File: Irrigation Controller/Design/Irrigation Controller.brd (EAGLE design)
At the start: 100 x 80 mm, 21 parts, among them IC1 7809DT, IC2 LM1117-3.3, IC3 7805DT, U1 ESP-WROOM-32, U4 MB6S

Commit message: Updated Schematics and Board
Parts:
- added D2, D3, D4, D5: (no value), diode:SOD123
- added JP1: Serial, SpaceDIY_connectors:1X04
- added OK1, OK2, OK3, OK4: SFH6186-4, optocoupler:SMD4-7
- added R10, R7, R8, R9: 470, resistor:R1206
- added R11: 10k, SpaceDIY_passive_components:1206
- added R3, R4, R5, R6: 10K, resistor:R1206
- added S3, S4, S5: 219-08, switch-dil:CTS-219-08
- added T1, T2, T3, T4: BC847, transistor:SOT23
- added U$6: SWITCH_SPDT, SparkFun-Retired:KPS-1290
- added X1, X2, X3, X4: 22-23-2021, con-molex:22-23-2021
- U1: value ESP-WROOM-32 -> ESP-32S; device esp32:ESP-WROOM-32 -> esp32:ESP-32S
- moved D1 188.2 mm to (21.0, 101.0)
- moved C6 149.5 mm to (54.0, 86.0)
- moved C2 148.9 mm to (41.0, 92.0)
- moved C3 148.9 mm to (47.0, 92.0)
- moved C5 148.9 mm to (47.0, 86.0)
- moved S2 2.83 mm to (13.0, 32.0)
- moved U$3 2.24 mm to (37.0, 17.0)
- moved U$2 1.41 mm to (13.0, 17.0)
- moved U$4 1.41 mm to (62.0, 17.0)
- moved U$5 1.00 mm to (86.0, 17.0)
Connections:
- removed net VCC: R2.2
- new net 2R1: S3.10, S3.11, S3.12, S3.14, S3.16, X2.1
- new net 2R2: S3.13, S3.15, S3.9, U$3.SWCOMMON
- new net 3R1: S4.10, S4.11, S4.12, S4.14, S4.16, X3.1
- new net 3R2: S4.13, S4.15, S4.9, U$4.SWCOMMON
- new net 4R1: S5.10, S5.11, S5.12, S5.14, S5.16, X4.1
- new net 4R2: S5.13, S5.15, S5.9, U$5.SWCOMMON
- new net CLK: U1.20
- new net CMD: U1.19
- new net IO0: R11.2, U$6.P, U1.25
- new net IO12: U1.14
- new net IO13: U1.16
- new net IO14: U1.13
- new net IO15: U1.23
- new net IO16: U1.27
- new net IO17: U1.28
- new net IO18: U1.30
- new net IO19: U1.31
- new net IO2: U1.24
- new net IO21: U1.33
- new net IO22: U1.36
- new net IO23: U1.37
- new net IO25: U1.10
- new net IO26: U1.11
- new net IO27: U1.12
- new net IO32: U1.8
- new net IO33: U1.9
- new net IO34: U1.6
- new net IO35: U1.7
- new net IO4: U1.26
- new net IO5: U1.29
- new net N$1: U$5.SWOPEN, X4.2
- new net N$10: D3.C, OK2.4, U$3.COIL1
- new net N$11: D3.A, T2.3, U$3.COIL0
- new net N$12: OK2.3, R4.2
- new net N$13: R4.1, T2.1
- new net N$14: D4.C, OK3.4, U$4.COIL1
- new net N$15: D4.A, T3.3, U$4.COIL0
- new net N$16: OK3.3, R5.2
- new net N$17: R5.1, T3.1
- new net N$18: D5.C, OK4.4, U$5.COIL1
- new net N$19: D5.A, T4.3, U$5.COIL0
- new net N$2: U$4.SWOPEN, X3.2
- new net N$20: OK4.3, R6.2
- new net N$21: R6.1, T4.1
- new net N$22: OK1.1, R7.1
- new net N$23: R7.2
- new net N$25: OK2.1, R8.1
- new net N$26: R8.2
- new net N$27: OK3.1, R9.1
- new net N$28: R9.2
- new net N$29: OK4.1, R10.1
- new net N$30: R10.2
- new net N$4: U$3.SWOPEN, X2.2
- new net N$5: U$2.SWOPEN, X1.2
- new net N$6: D2.C, OK1.4, U$2.COIL1
- new net N$7: D2.A, T1.3, U$2.COIL0
- new net N$8: OK1.3, R3.2
- new net N$9: R3.1, T1.1
- new net RX: JP1.1, U1.34
- new net SD0: U1.21
- new net SD1: U1.22
- new net SD2: U1.17
- new net SD3: U1.18
- new net SVN: U1.5
- new net SVP: U1.4
- new net TX: JP1.2, U1.35
- net 1R1: now also X1.1
- net 1R2: now also U$2.SWCOMMON
- net 24V1: now also S3.3, S4.3, S5.3
- net 24V2: now also S3.4, S4.4, S5.4
- net 3V3: now also R11.1, R2.2, S3.7, S4.7, S5.7
- net 5V: now also JP1.4, S3.6, S4.6, S5.6
- net 9V: now also S3.5, S4.5, S5.5
- net AC1: now also S3.1, S4.1, S5.1
- net AC2: now also S3.2, S4.2, S5.2
- net GND: now also JP1.3, OK1.2, OK2.2, OK3.2, OK4.2, S3.8, S4.8, S5.8, T1.2, T2.2, T3.2, T4.2, U$6.O
- net RST: now also U1.3

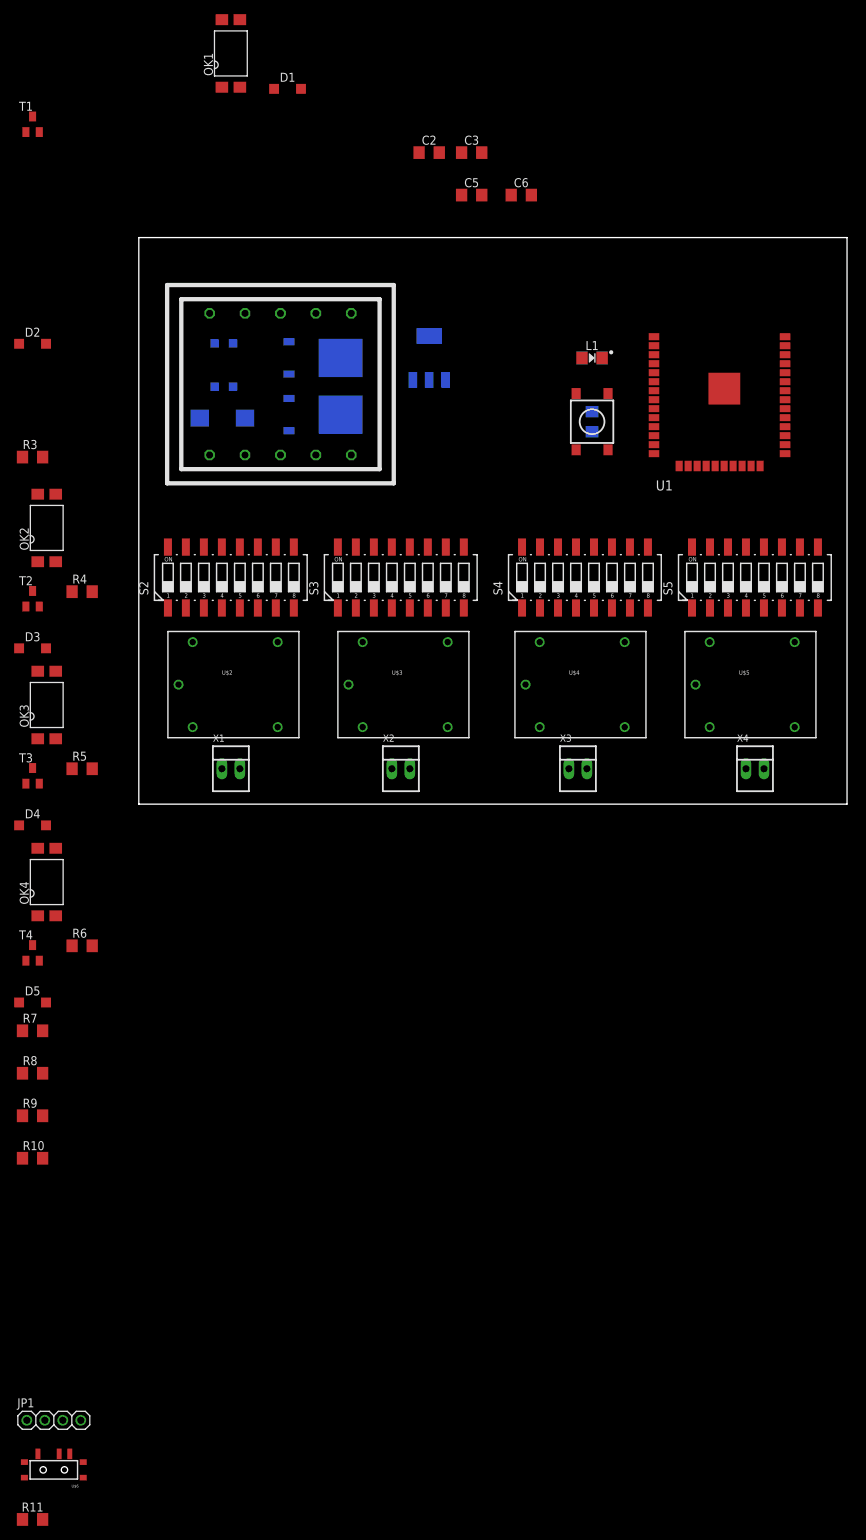
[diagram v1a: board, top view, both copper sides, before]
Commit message: Irrigation controller with support for:  * 220 VAC  * 24 VAC  * 9 VDC  * 5 VDC  * 3.3 VDC
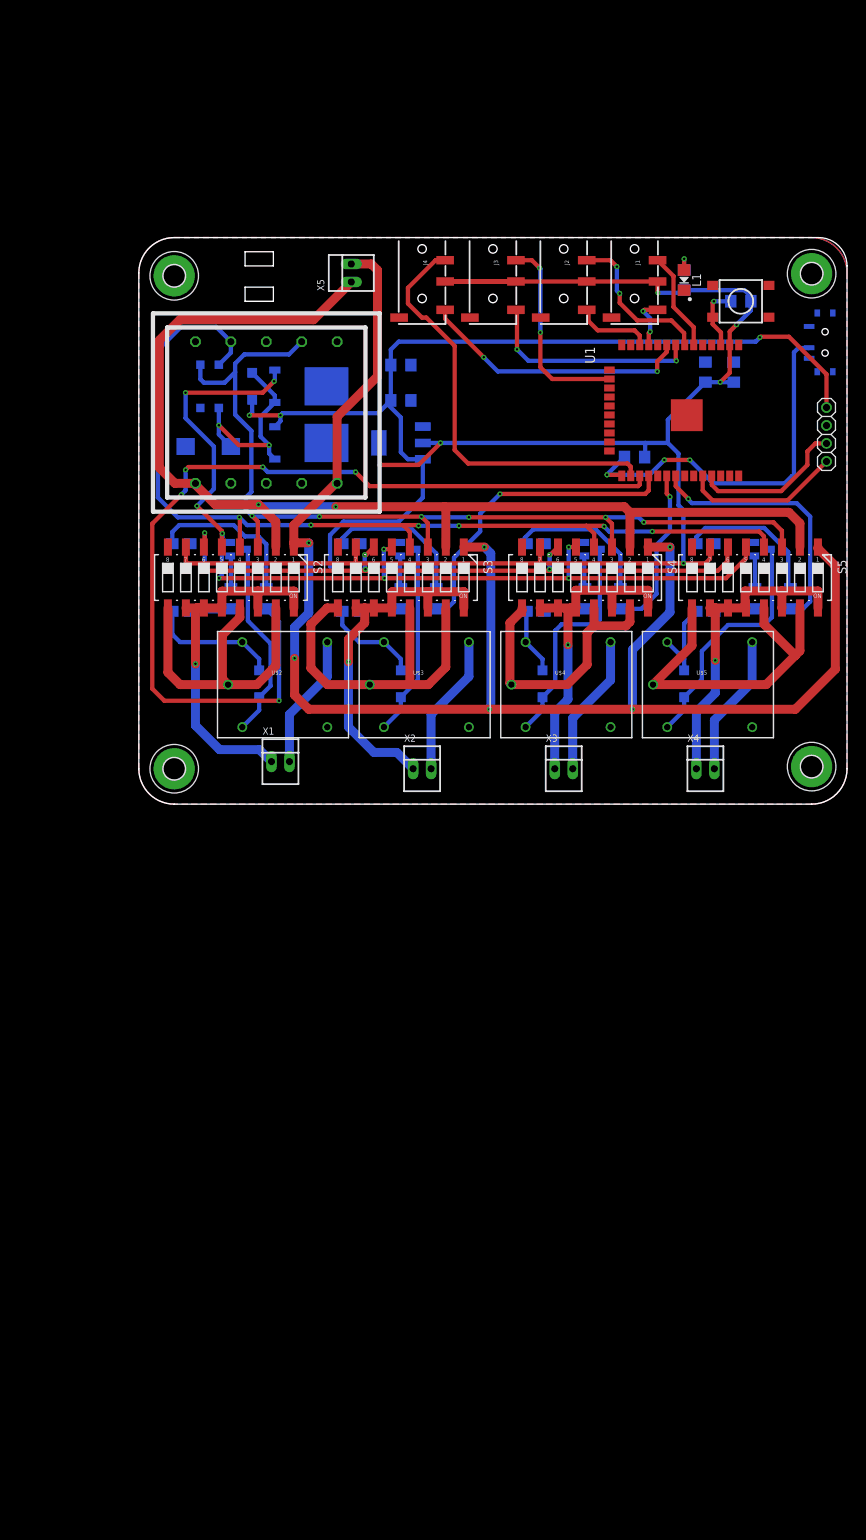
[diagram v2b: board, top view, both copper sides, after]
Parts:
- removed C6: 22uF, SpaceDIY_passive_components:1206
- added C1: 100uF, resistor:CT7343
- added H1, H2, H3, H4: MOUNT-PAD-ROUND3.0, holes:3,0-PAD
- added J1, J2, J3, J4: AUDIO_JACK_TRRSSMD_RA, SparkFun-Connectors:AUDIO_JACK_3.5MM_TRRS_SMD_RA
- added X5: 22-23-2021, con-molex:22-23-2021
- C3: value 100nF -> 22uF
- C4: value 100uF -> 100nF; device resistor:CT7343 -> SpaceDIY_passive_components:1206
- moved U$6 192.9 mm to (96.9, 65.2), flipped to the bottom, turned to 270 degrees
- moved JP1 176.9 mm to (97.1, 52.2), turned to 90 degrees
- moved R11 172.4 mm to (70.0, 49.0), flipped to the bottom
- moved R10 133.0 mm to (92.0, 29.0), flipped to the bottom, turned to 270 degrees
- moved T4 117.7 mm to (88.0, 36.0), flipped to the bottom, turned to 90 degrees
- moved R9 110.5 mm to (68.0, 29.0), flipped to the bottom, turned to 270 degrees
- moved R6 106.9 mm to (87.0, 29.0), flipped to the bottom, turned to 270 degrees
- moved OK4 102.5 mm to (80.0, 32.0), flipped to the bottom, turned to 180 degrees
- moved D5 102.4 mm to (77.0, 17.0), flipped to the bottom, turned to 270 degrees
- moved R8 88.0 mm to (42.0, 29.0), flipped to the bottom, turned to 270 degrees
- moved T3 85.2 mm to (64.0, 36.0), flipped to the bottom, turned to 90 degrees
- moved R5 74.9 mm to (63.0, 29.0), flipped to the bottom, turned to 270 degrees
- moved D4 74.7 mm to (57.0, 17.0), flipped to the bottom, turned to 270 degrees
- moved OK1 74.3 mm to (6.00, 32.0), flipped to the bottom, turned to 180 degrees
- moved C4 72.5 mm to (84.0, 61.0), turned to 90 degrees
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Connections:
- removed net N$23: R7.2
- removed net N$26: R8.2
- removed net N$28: R9.2
- removed net N$30: R10.2
- net 24VDC: now also C1.+; no longer C4.+
- net 3V3: now also C4.1, C5.1, J1.RING1, J2.RING1, J3.RING1, J4.RING1; no longer C3.1, C6.1
- net 5V: now also C3.1; no longer C5.1
- net AC1: now also U$1.P2, X5.2; no longer U$1.P1
- net AC2: now also U$1.P1, X5.1; no longer U$1.P2
- net GND: now also C1.-, C4.2, H1.B3,0, H2.B3,0, H3.B3,0, H4.B3,0, J1.EARTH, J2.EARTH, J3.EARTH, J4.EARTH; no longer C4.-, C6.2
- net IO13: now also J3.RING2
- net IO16: now also R7.2
- net IO17: now also R8.2
- net IO18: now also R9.2
- net IO19: now also R10.2
- net IO26: now also J1.TIP
- net IO27: now also J2.TIP
- net IO32: now also J3.TIP
- net IO33: now also J4.TIP
- net IO34: now also J1.RING2
- net IO35: now also J2.RING2
- net IO4: now also J4.RING2
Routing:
- net 3V3: track 0.00 -> 234.3 mm, vias 0 -> 6
- net 5V: track 0.00 -> 230.1 mm, vias 0 -> 10
- net AC1: track 0.00 -> 224.9 mm, vias 0 -> 6
- net AC2: track 0.00 -> 163.4 mm, vias 0 -> 2
- net 24V2: track 0.00 -> 137.9 mm, vias 0 -> 6
- net 9V: track 0.00 -> 135.3 mm, vias 0 -> 9
- net 24V1: track 0.00 -> 133.6 mm, vias 0 -> 6
- net IO16: track 0.00 -> 131.9 mm, vias 0 -> 5
- net IO4: track 0.00 -> 60.0 mm
- net IO0: track 0.00 -> 54.5 mm, vias 0 -> 3
- net 1R1: track 0.00 -> 52.9 mm, vias 0 -> 1
- net 2R1: track 0.00 -> 51.7 mm, vias 0 -> 1
- net 2R2: track 0.00 -> 51.2 mm
- net 4R2: track 0.00 -> 50.4 mm
- net 4R1: track 0.00 -> 47.1 mm, vias 0 -> 1
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- added copper zone on layer 1, net GND
- added copper zone on layer 16, net GND
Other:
- outline, holes or cut-outs redrawn

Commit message: Addapted SCH and BRD to work with low-voltage on the outputs
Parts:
- S2, S3, S4, S5: value 219-08 -> 219-06; device switch-dil:CTS-219-08 -> switch-dil:CTS-219-06
- moved D5 20.6 mm to (87.0, 35.0), turned to 90 degrees
- moved D4 19.3 mm to (64.0, 35.0), turned to 90 degrees
- moved D3 18.2 mm to (40.0, 35.0), turned to 90 degrees
- moved D2 18.0 mm to (17.0, 35.0), turned to 90 degrees
- moved T1 7.07 mm to (21.0, 35.0)
- moved T2 6.08 mm to (44.0, 35.0)
- moved T3 4.12 mm to (68.0, 35.0)
- moved OK1 4.00 mm to (10.0, 32.0)
- moved R3 4.00 mm to (17.0, 29.0)
- moved T4 3.16 mm to (91.0, 35.0)
- moved OK2 3.00 mm to (33.0, 32.0)
- moved R4 3.00 mm to (40.0, 29.0)
- moved R7 3.00 mm to (21.0, 29.0)
- moved R8 2.00 mm to (44.0, 29.0)
- moved S2 2.00 mm to (15.0, 32.0)
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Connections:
- net 1R1: now also S2.8, S2.9; no longer S2.11, S2.14, S2.16
- net 1R2: now also S2.11, S2.7; no longer S2.13, S2.15, S2.9
- net 24V1: now also S2.1, S3.1, S4.1, S5.1; no longer S2.3, S3.3, S4.3, S5.3
- net 24V2: now also S2.2, S3.2, S4.2, S5.2; no longer S2.4, S3.4, S4.4, S5.4
- net 2R1: now also S3.8, S3.9; no longer S3.11, S3.14, S3.16
- net 2R2: now also S3.11, S3.7; no longer S3.13, S3.15, S3.9
- net 3R1: now also S4.8, S4.9; no longer S4.11, S4.14, S4.16
- net 3R2: now also S4.11, S4.7; no longer S4.13, S4.15, S4.9
- net 3V3: now also S2.5, S3.5, S4.5, S5.5; no longer S2.7, S3.7, S4.7, S5.7
- net 4R1: now also S5.8, S5.9; no longer S5.11, S5.14, S5.16
- net 4R2: now also S5.11, S5.7; no longer S5.13, S5.15, S5.9
- net 5V: now also S2.4, S3.4, S4.4, S5.4; no longer S2.6, S3.6, S4.6, S5.6
- net 9V: now also S2.3, S3.3, S4.3, S5.3; no longer S2.5, S3.5, S4.5, S5.5
- net AC1: no longer S2.1, S3.1, S4.1, S5.1
- net AC2: no longer S2.2, S3.2, S4.2, S5.2
- net GND: now also S2.6, S3.6, S4.6, S5.6; no longer S2.8, S3.8, S4.8, S5.8
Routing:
- net AC1: track 224.9 -> 36.5 mm, vias 6 -> 0
- net AC2: track 163.4 -> 54.5 mm, vias 2 -> 0
- net IO16: track 131.9 -> 63.2 mm, vias 5 -> 1
- net 2R2: track 51.2 -> 29.6 mm
- net 4R2: track 50.4 -> 30.7 mm
- net 1R2: track 46.5 -> 28.1 mm
- net N$11: track 27.2 -> 45.3 mm, vias 0 -> 1
- net 1R1: track 52.9 -> 35.4 mm, vias 1 -> 2
- net 24V2: track 137.9 -> 121.5 mm, vias 6 -> 0
- net N$14: track 9.37 -> 24.6 mm, vias 0 -> 2
- net 2R1: track 51.7 -> 38.9 mm, vias 1 -> 2
- net N$19: track 34.4 -> 46.0 mm, vias 0 -> 1
- net 3V3: track 234.3 -> 222.9 mm
- net N$7: track 28.2 -> 39.3 mm, vias 0 -> 1
- net N$15: track 32.2 -> 43.1 mm, vias 0 -> 1
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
